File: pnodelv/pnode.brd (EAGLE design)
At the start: 50 x 23 mm, 41 parts, among them IC2 HTU21D, IC3 SI4012

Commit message: Routing for pnodelv
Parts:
- added U$4: 4.7u, jonsowman:BOURNS_SDE0403A
- moved C3 34.8 mm to (34.5, 3.05), turned to 270 degrees
- moved U$2 31.8 mm to (31.2, 3.05), turned to 90 degrees
- moved R10 27.0 mm to (27.4, 2.79), turned to 90 degrees
- moved C10 25.6 mm to (22.9, 2.79), turned to 270 degrees
- moved R9 24.0 mm to (25.1, 2.79), turned to 270 degrees
- moved JP1 7.66 mm to (39.9, 3.05), turned to 180 degrees
- moved R7 0.51 mm to (31.8, 7.62)
- moved R8 0.51 mm to (29.5, 7.62)
- moved C13 0.51 mm to (34.0, 7.62)
- moved C2 0.25 mm to (20.6, 2.79)
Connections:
- new net N$6: U$2.1, U$4.P$2
- net GND: now also JP1.1
- net VBATT: now also U$4.P$1
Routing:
- net N$6: track 0.00 -> 16.8 mm
- net VBATT: track 0.08 -> 16.4 mm
- net +3V3: track 80.5 -> 90.6 mm
- net N$3: track 0.00 -> 5.11 mm
- net GND: track 17.9 -> 12.9 mm, vias 50 -> 51
- net VBATT_MEAS: track 13.7 -> 13.2 mm
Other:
- board text added: "1.5V"
- board text added: "pNodeLV"
- board text removed: "UKHASnet"

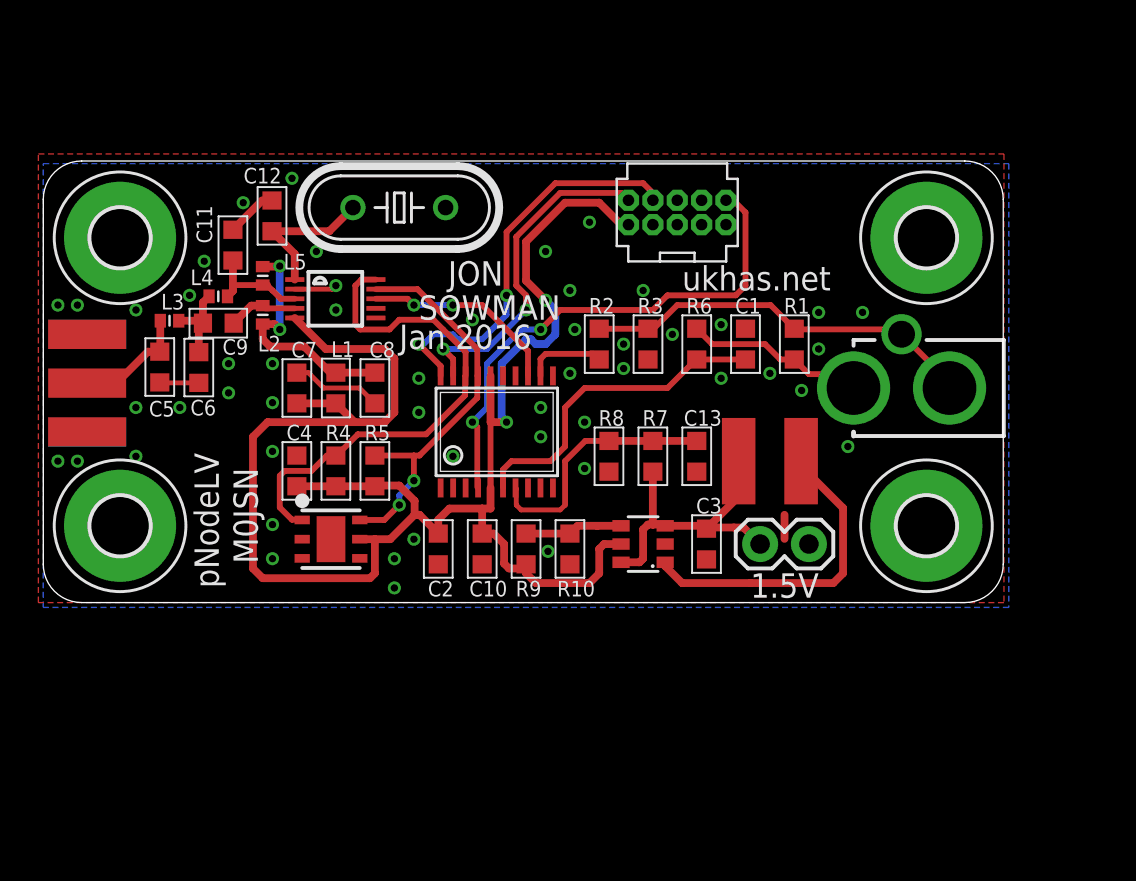
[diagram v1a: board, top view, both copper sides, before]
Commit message: Added silk and submitted gerbers for pnodelv
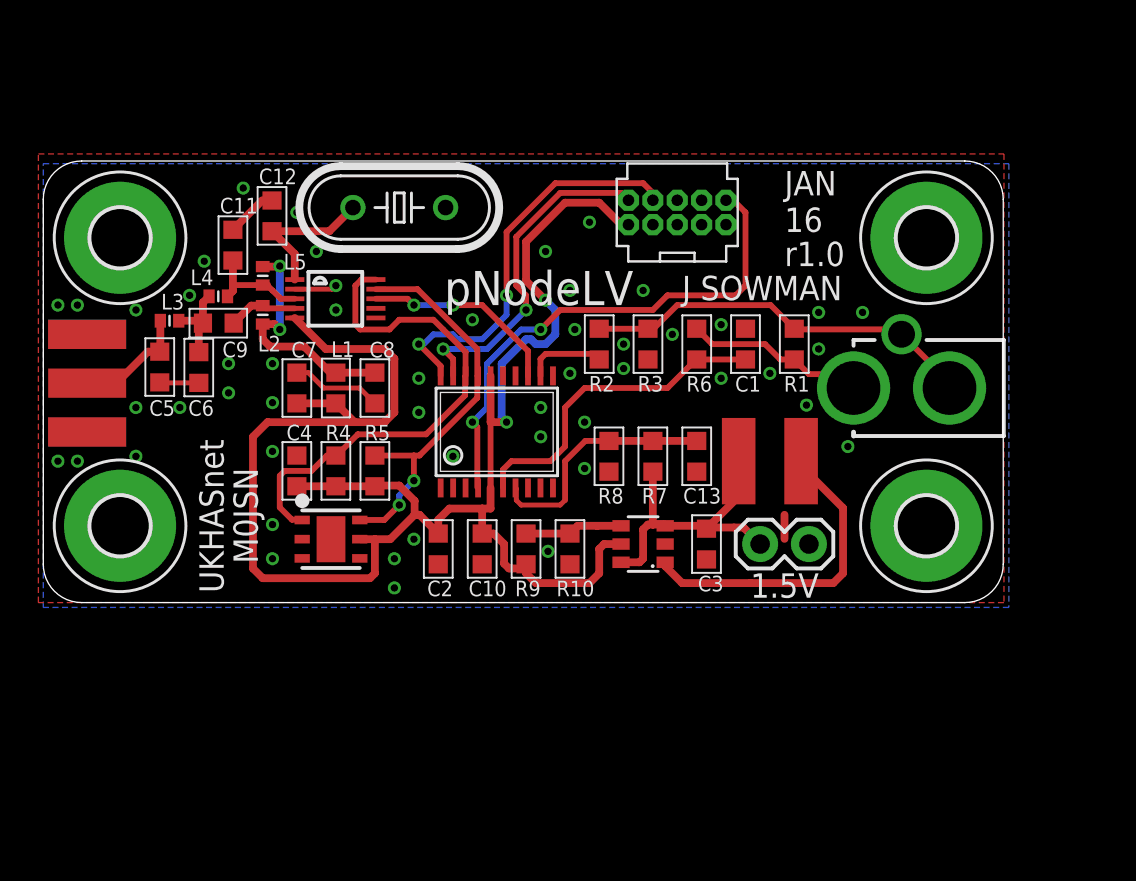
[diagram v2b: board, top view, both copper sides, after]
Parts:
- R10: value 1M -> 562k
- R9: value 1M -> 976k
- renumbered U$4 to L6
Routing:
- net VBATT_MEAS: track 13.2 -> 12.7 mm
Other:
- board text added: "J SOWMAN"
- board text added: "JAN 16"
- board text added: "UKHASnet"
- board text added: "jonsowman.com"
- board text added: "r1.0"
- board text removed: "JON"
- board text removed: "Jan 2016"
- board text removed: "SOWMAN"
- board text removed: "ukhas.net"

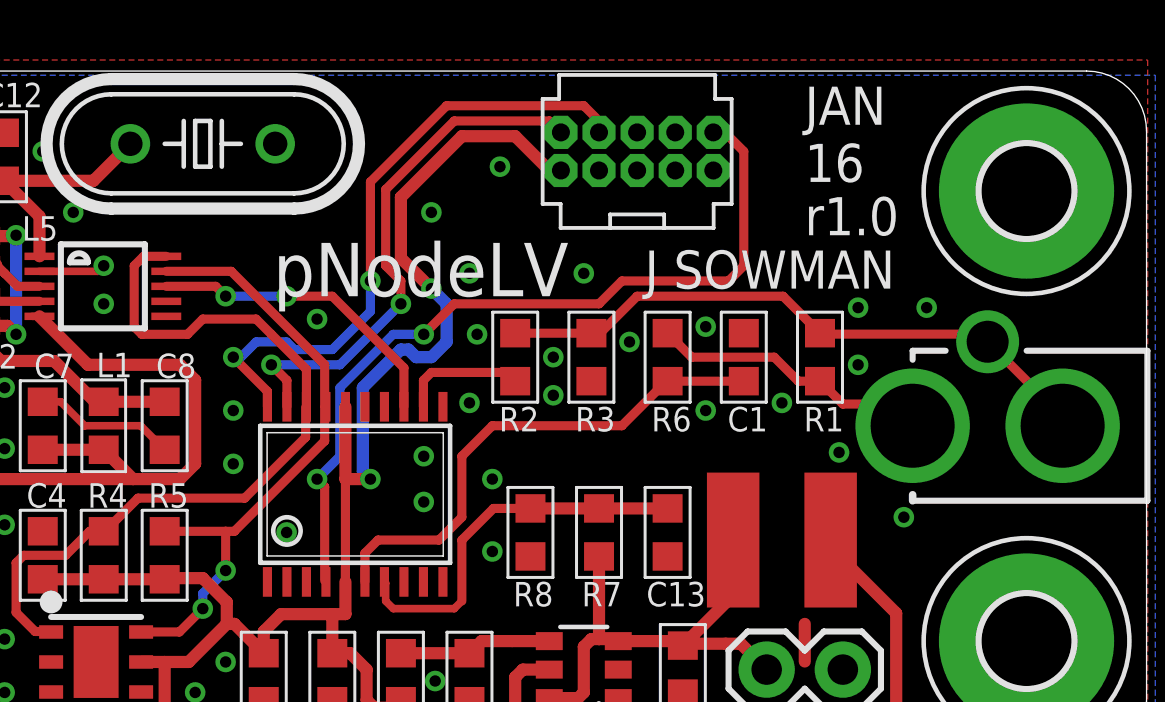
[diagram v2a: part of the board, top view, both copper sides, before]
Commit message: switched to smd swd header
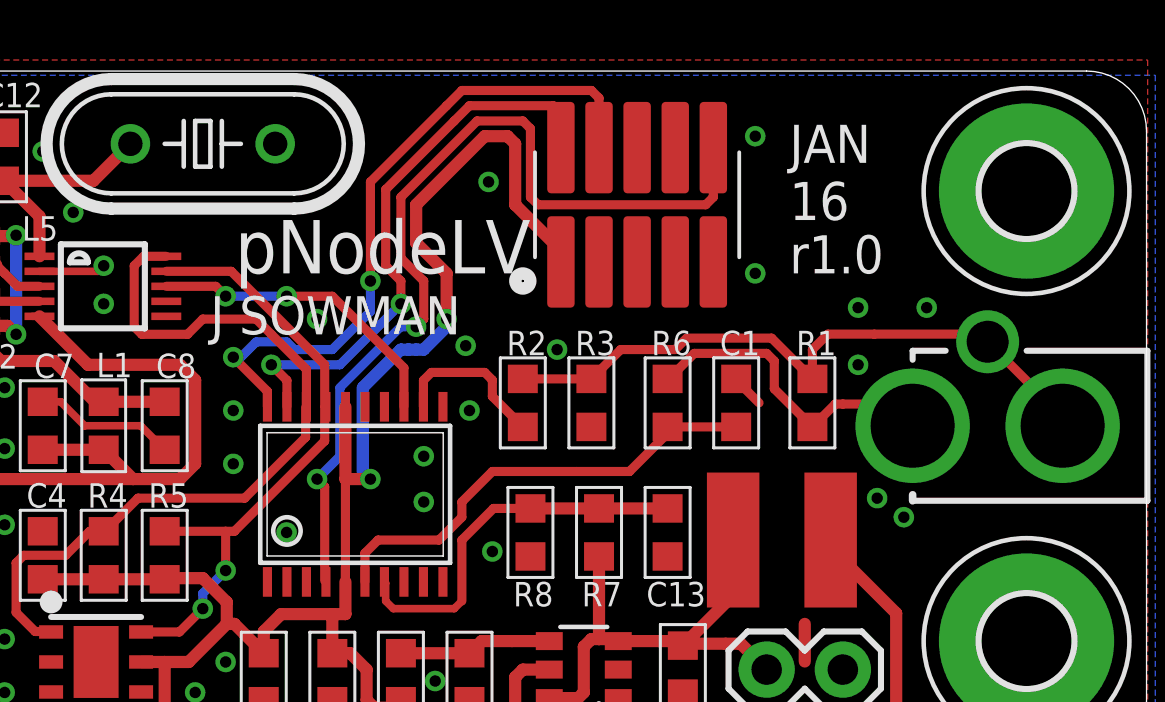
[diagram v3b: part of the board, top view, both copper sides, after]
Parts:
- removed U$3: SWD_PTH_SHROUD, jonsowman:SWD_PTH_SHROUD
- added J1: SWD_SHROUD_SMD, dtb:SWD_SMD_SHROUD
- moved R2 1.55 mm to (29.2, 11.9)
- moved C1 1.55 mm to (36.3, 11.9)
- moved R1 1.55 mm to (38.9, 11.9)
- moved R3 1.52 mm to (31.5, 11.9)
- moved R6 1.52 mm to (34.0, 11.9)
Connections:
- net +3V3: now also J1.1; no longer U$3.1
- net GND: now also J1.3, J1.5, J1.7, J1.9; no longer U$3.3, U$3.5, U$3.7, U$3.9
- net NRST: now also J1.10; no longer U$3.10
- net SWCLK: now also J1.4; no longer U$3.4
- net SWDAT: now also J1.2; no longer U$3.2
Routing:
- net NRST: track 27.1 -> 30.8 mm
- net CLAMP: track 17.2 -> 15.5 mm
- net +3V3: track 90.6 -> 92.0 mm
- net SWCLK: track 21.1 -> 22.5 mm
- net N$1: track 9.45 -> 10.7 mm
- net SWDAT: track 17.7 -> 19.0 mm
- net CLAMP_POWER: track 4.17 -> 5.38 mm
- net GND: track 12.9 -> 14.0 mm, vias 51 -> 44
- net N$2: track 20.7 -> 21.8 mm

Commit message: tidying silk again
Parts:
- moved J1 0.51 mm to (33.5, 18.5)
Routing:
- net +3V3: track 92.0 -> 92.6 mm
- net SWCLK: track 22.5 -> 23.0 mm
- net SWDAT: track 19.0 -> 19.6 mm
- net NRST: track 30.8 -> 31.3 mm
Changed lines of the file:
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@@
 <wire x1="50" y1="21" x2="48" y2="23" width="0" layer="20" curve="90"/>
 <text x="11.176" y="2.032" size="1.27" layer="21" font="vector" ratio="15" rot="R90">M0JSN</text>
-<text x="18.796" y="14.224" size="1.27" layer="21" font="vector" ratio="15">J SOWMAN</text>
-<text x="38.1" y="18.034" size="1.27" layer="21" font="vector" ratio="15">JAN
+<text x="18.796" y="13.97" size="1.27" layer="21" font="vector" ratio="15">J SOWMAN</text>
+<text x="38.354" y="18.034" size="1.27" layer="21" font="vector" ratio="15">JAN
 16</text>
 <text x="9.398" y="0.508" size="1.27" layer="21" font="vector" ratio="15" rot="R90">UKHASnet</text>
 <text x="36.83" y="0.254" size="1.27" layer="21" font="vector" ratio="15">1.5V</text>
-<text x="29.464" y="18.034" size="1.778" layer="21" font="vector" ratio="15" rot="R180">pNodeLV</text>
+<text x="29.718" y="17.78" size="1.778" layer="21" font="vector" ratio="15" rot="R180">pNodeLV</text>
 <text x="33.02" y="5.842" size="2.54" layer="22" font="vector" ratio="15" rot="MR0">pNodeLV</text>
 <text x="34.544" y="1.778" size="2.54" layer="22" font="vector" ratio="15" rot="MR0">J SOWMAN</text>
 <text x="9.652" y="18.542" size="1.27" layer="22" font="vector" ratio="15" rot="MR270">jonsowman.com</text>
-<text x="38.1" y="16.256" size="1.27" layer="21" font="vector" ratio="15">r1.0</text>
+<text x="38.354" y="16.256" size="1.27" layer="21" font="vector" ratio="15">r1.0</text>
 </plain>
 <attributes>
@@
 </element>
 <element name="L6" library="jonsowman" package="BOURNS_SDE0403A" value="4.7u" x="37.846" y="7.366"/>
-<element name="J1" library="dtb" package="SWD_SMD_SHROUD" value="SWD_SHROUD_SMD" x="33.02" y="18.542"/>
+<element name="J1" library="dtb" package="SWD_SMD_SHROUD" value="SWD_SHROUD_SMD" x="33.528" y="18.542"/>
 </elements>
 <signals>
@@
 <wire x1="36.322" y1="12.738" x2="36.322" y2="12.7" width="0.3048" layer="1"/>
 <wire x1="36.322" y1="12.7" x2="37.084" y2="11.938" width="0.3048" layer="1"/>
-<via x="28.067" y="19.304" extent="1-16" drill="0.381"/>
+<via x="28.575" y="19.812" extent="1-16" drill="0.381"/>
 <via x="27.305" y="13.843" extent="1-16" drill="0.381"/>
-<via x="36.957" y="20.828" extent="1-16" drill="0.381"/>
-<via x="36.957" y="16.256" extent="1-16" drill="0.381"/>
+<via x="37.465" y="20.828" extent="1-16" drill="0.381"/>
+<via x="37.465" y="16.256" extent="1-16" drill="0.381"/>
 </signal>
 <signal name="+3V3">
@@
 <wire x1="25.108" y1="1.956" x2="25.146" y2="1.994" width="0.4064" layer="1"/>
 <contactref element="J1" pad="1"/>
-<wire x1="30.48" y1="16.637" x2="30.48" y2="16.764" width="0.4064" layer="1"/>
-<wire x1="30.48" y1="16.637" x2="30.48" y2="17.018" width="0.4064" layer="1"/>
-<wire x1="30.48" y1="17.018" x2="28.956" y2="18.542" width="0.4064" layer="1"/>
-<wire x1="28.956" y1="18.542" x2="28.956" y2="20.574" width="0.4064" layer="1"/>
-<wire x1="28.956" y1="20.574" x2="28.702" y2="20.828" width="0.4064" layer="1"/>
-<wire x1="28.702" y1="20.828" x2="27.94" y2="20.828" width="0.4064" layer="1"/>
+<wire x1="30.48" y1="17.018" x2="29.718" y2="17.78" width="0.4064" layer="1"/>
+<wire x1="29.718" y1="17.78" x2="29.718" y2="20.574" width="0.4064" layer="1"/>
+<wire x1="29.718" y1="20.574" x2="29.464" y2="20.828" width="0.4064" layer="1"/>
+<wire x1="29.464" y1="20.828" x2="27.94" y2="20.828" width="0.4064" layer="1"/>
 <wire x1="27.94" y1="20.828" x2="25.654" y2="18.542" width="0.4064" layer="1"/>
 <wire x1="25.654" y1="18.542" x2="25.654" y2="17.272" width="0.4064" layer="1"/>
@@
 <via x="26.67" y="14.732" extent="1-16" drill="0.381"/>
 <wire x1="26.67" y1="14.732" x2="26.67" y2="14.478" width="0.4064" layer="16"/>
+<wire x1="30.988" y1="16.637" x2="30.861" y2="16.637" width="0.4064" layer="1"/>
+<wire x1="30.861" y1="16.637" x2="30.48" y2="17.018" width="0.4064" layer="1"/>
 </signal>
 <signal name="SCL">
@@
 <contactref element="J1" pad="2"/>
 <wire x1="26.924" y1="21.336" x2="27.432" y2="21.844" width="0.3048" layer="1"/>
-<wire x1="27.432" y1="21.844" x2="30.226" y2="21.844" width="0.3048" layer="1"/>
-<wire x1="30.226" y1="21.844" x2="30.48" y2="21.59" width="0.3048" layer="1"/>
-<wire x1="30.48" y1="21.59" x2="30.48" y2="20.447" width="0.3048" layer="1"/>
+<wire x1="27.432" y1="21.844" x2="30.734" y2="21.844" width="0.3048" layer="1"/>
+<wire x1="30.734" y1="21.844" x2="30.988" y2="21.59" width="0.3048" layer="1"/>
+<wire x1="30.988" y1="21.59" x2="30.988" y2="20.447" width="0.3048" layer="1"/>
 </signal>
 <signal name="SWCLK">
@@
 <contactref element="J1" pad="4"/>
 <wire x1="26.67" y1="21.844" x2="27.178" y2="22.352" width="0.3048" layer="1"/>
-<wire x1="27.178" y1="22.352" x2="31.496" y2="22.352" width="0.3048" layer="1"/>
-<wire x1="31.496" y1="22.352" x2="31.75" y2="22.098" width="0.3048" layer="1"/>
-<wire x1="31.75" y1="22.098" x2="31.75" y2="20.447" width="0.3048" layer="1"/>
+<wire x1="27.178" y1="22.352" x2="32.004" y2="22.352" width="0.3048" layer="1"/>
+<wire x1="32.004" y1="22.352" x2="32.258" y2="22.098" width="0.3048" layer="1"/>
+<wire x1="32.258" y1="22.098" x2="32.258" y2="20.447" width="0.3048" layer="1"/>
 </signal>
 <signal name="NRST">
@@
 <wire x1="25.146" y1="16.764" x2="25.146" y2="18.796" width="0.3048" layer="1"/>
 <wire x1="25.146" y1="18.796" x2="27.686" y2="21.336" width="0.3048" layer="1"/>
-<wire x1="27.686" y1="21.336" x2="29.21" y2="21.336" width="0.3048" layer="1"/>
-<wire x1="29.21" y1="21.336" x2="29.464" y2="21.082" width="0.3048" layer="1"/>
-<wire x1="29.464" y1="21.082" x2="29.464" y2="18.796" width="0.3048" layer="1"/>
-<wire x1="29.464" y1="18.796" x2="29.718" y2="18.542" width="0.3048" layer="1"/>
-<wire x1="29.718" y1="18.542" x2="35.306" y2="18.542" width="0.3048" layer="1"/>
-<wire x1="35.306" y1="18.542" x2="35.56" y2="18.796" width="0.3048" layer="1"/>
-<wire x1="35.56" y1="18.796" x2="35.56" y2="20.447" width="0.3048" layer="1"/>
+<wire x1="27.686" y1="21.336" x2="29.972" y2="21.336" width="0.3048" layer="1"/>
+<wire x1="29.972" y1="21.336" x2="30.226" y2="21.082" width="0.3048" layer="1"/>
+<wire x1="30.226" y1="21.082" x2="30.226" y2="18.796" width="0.3048" layer="1"/>
+<wire x1="30.226" y1="18.796" x2="30.48" y2="18.542" width="0.3048" layer="1"/>
+<wire x1="30.48" y1="18.542" x2="35.814" y2="18.542" width="0.3048" layer="1"/>
+<wire x1="35.814" y1="18.542" x2="36.068" y2="18.796" width="0.3048" layer="1"/>
+<wire x1="36.068" y1="18.796" x2="36.068" y2="20.447" width="0.3048" layer="1"/>
 <wire x1="25.908" y1="16.002" x2="25.908" y2="14.732" width="0.3048" layer="1"/>
 <wire x1="25.908" y1="14.732" x2="25.654" y2="14.478" width="0.3048" layer="1"/>
